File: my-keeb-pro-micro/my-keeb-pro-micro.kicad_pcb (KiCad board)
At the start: 2 copper layers, 190.5 x 95.2 mm, 108 parts, among them SW1 SW_Push, U1 ATmega32U4-AU, Y1 16MHz

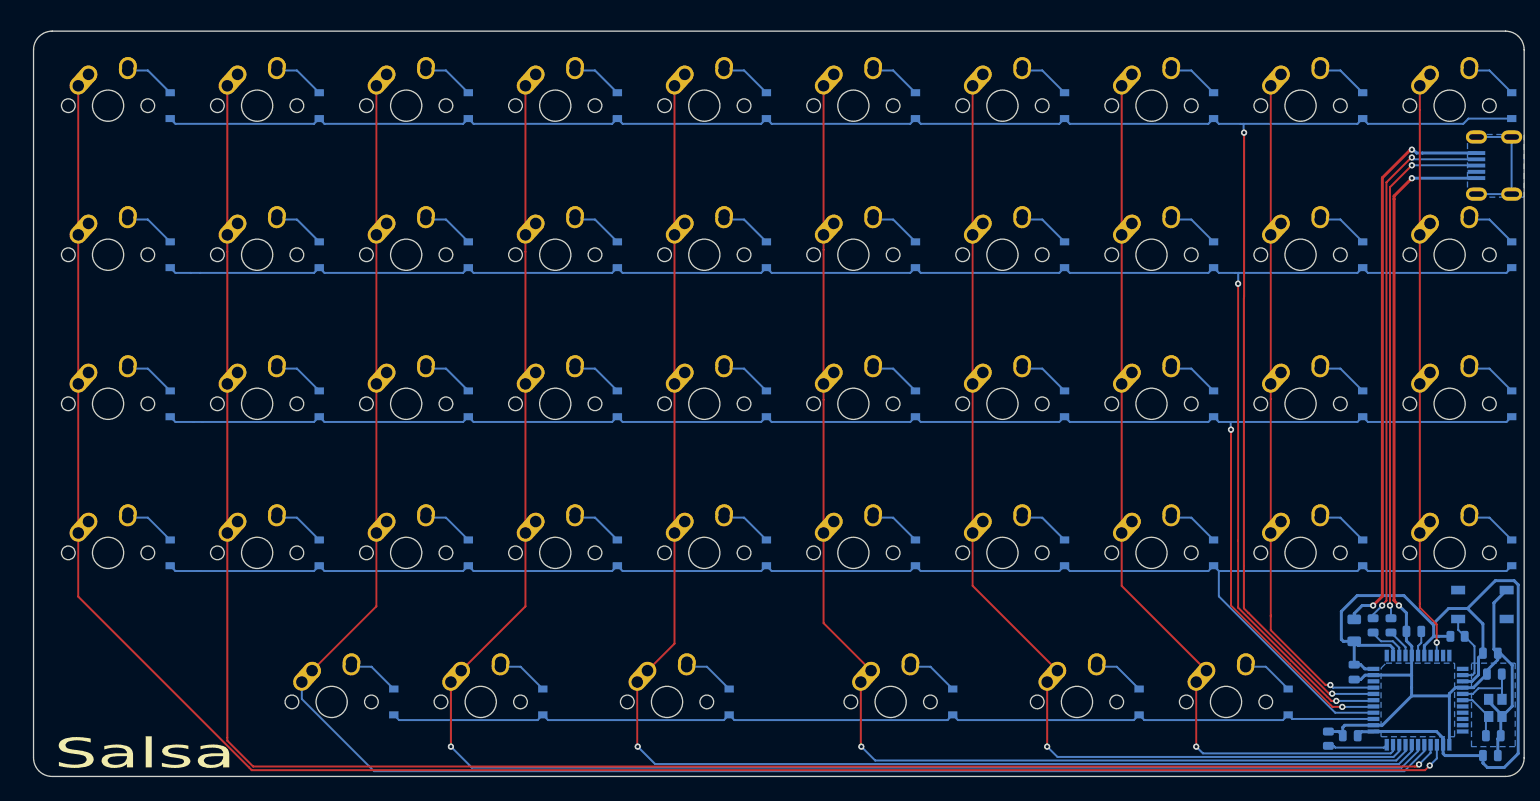
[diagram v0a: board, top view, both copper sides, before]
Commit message: Updated my-keeb pcb
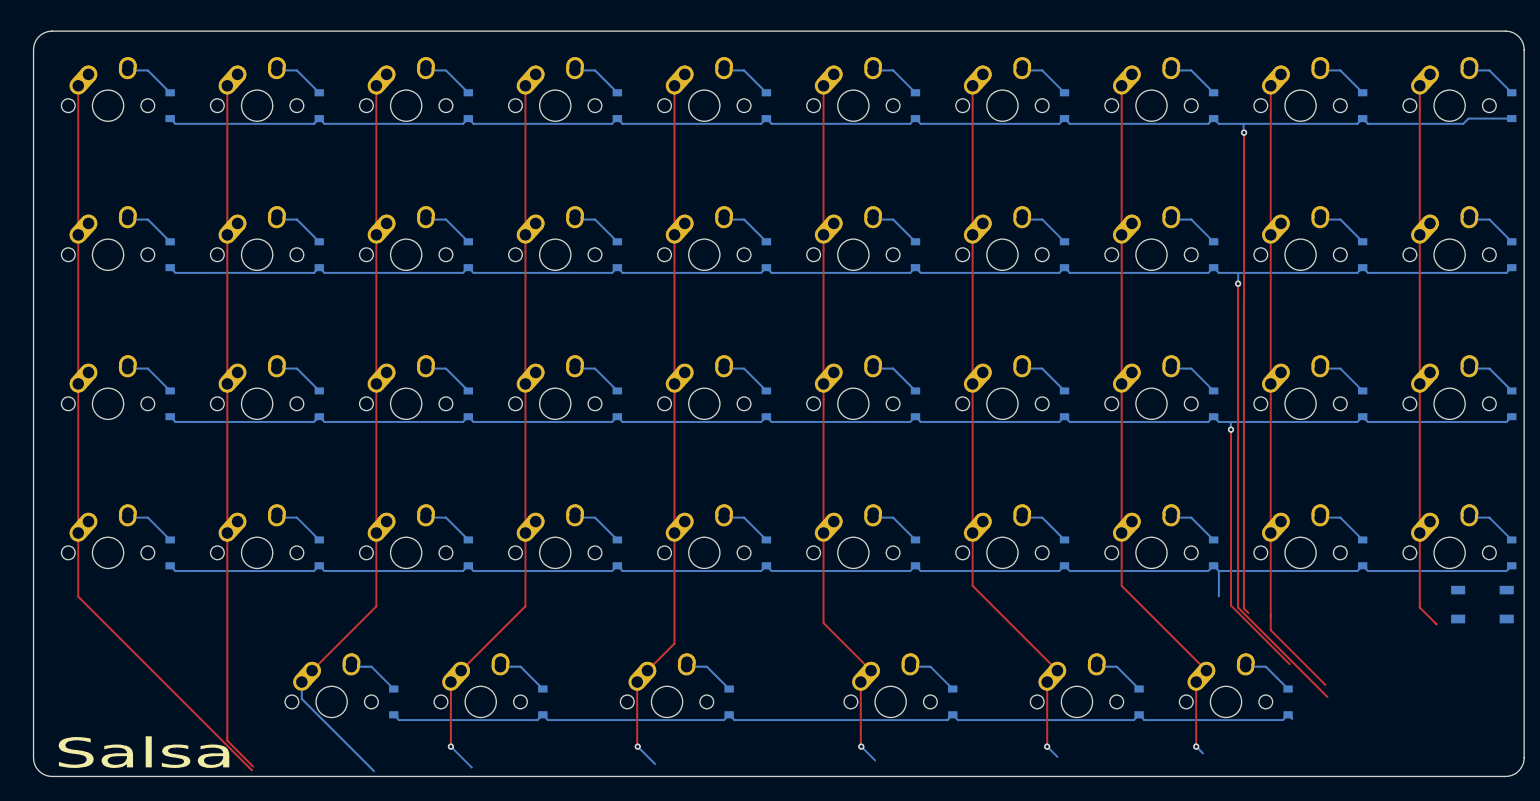
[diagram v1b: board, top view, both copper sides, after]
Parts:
- removed C1, C2, C5: 0.1uF, Capacitor_SMD:C_0805_2012Metric
- removed C3, C4: 22pF, Capacitor_SMD:C_0805_2012Metric
- removed C6: 1uF, Capacitor_SMD:C_0805_2012Metric
- removed C7: 10uF, Capacitor_SMD:C_0805_2012Metric
- removed F1: 500mA, Fuse:Fuse_1206_3216Metric
- removed R1, R2: 22, Resistor_SMD:R_0805_2012Metric
- removed R3, R4: 10k, Resistor_SMD:R_0805_2012Metric
- removed U1: ATmega32U4-AU, Package_QFP:TQFP-44_10x10mm_P0.8mm
- removed USB1: Molex-0548190589, random-keyboard-parts:Molex-0548190589
- removed Y1: 16MHz, Crystal:Crystal_SMD_3225-4Pin_3.2x2.5mm
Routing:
- net COL0: track 250.5 -> 96.6 mm, vias 1 -> 0
- net COL1: track 240.6 -> 88.4 mm, vias 1 -> 0
- net GND: track 144.9 -> 0.00 mm, vias 2 -> 0
- net COL2: track 229.5 -> 93.4 mm
- net COL3: track 212.8 -> 90.2 mm
- net +5V: track 110.1 -> 0.00 mm
- net COL4: track 185.8 -> 87.6 mm
- net VCC: track 72.6 -> 0.00 mm, vias 2 -> 0
- net D-: track 69.3 -> 0.00 mm, vias 2 -> 0
- net COL5: track 157.1 -> 88.0 mm
- net D+: track 67.4 -> 0.00 mm, vias 2 -> 0
- net COL6: track 134.2 -> 89.3 mm
- net ROW3: track 205.6 -> 179.7 mm
- net COL7: track 113.9 -> 88.7 mm
- net ROW0: track 259.5 -> 239.2 mm, vias 2 -> 1
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- removed copper zone on B.Cu, net GND

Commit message: Added pro micro to pcb, routing WIP
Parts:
- added U1: ProMicro, promicro:ProMicro, B.Cu at (117.5, 28.6)
- SW1: moved to F.Cu
- moved SW1 15.3 mm to (188.9, 98.4)
- moved D24 9.69 mm to (117.5, 27.8), turned to 0 degrees
- moved D25 9.69 mm to (117.5, 46.8), turned to 0 degrees
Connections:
- SW1 pad 1: GND -> Net-(SW1-Pad1)
- SW1 pad 2: Net-(R3-Pad2) -> GND
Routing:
- net ROW1: track 235.4 -> 239.2 mm
- net ROW0: track 239.2 -> 243.0 mm, vias 1 -> 3
- net Net-(D24-Pad2): track 6.62 -> 10.4 mm
- net Net-(D25-Pad2): track 6.62 -> 10.4 mm

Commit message: Added some footprints prettys
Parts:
- D45: footprint Diode_SMD:D_SOD-123 -> random-keyboard-parts:D_SOD-123-Pretty
- moved SW1 120.2 mm to (88.9, 31.8)
- moved D24 3.29 mm to (120.7, 26.9), turned to 90 degrees
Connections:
- U1 pad 19: ROW0 -> Net-(U1-Pad19)
- U1 pad 20: Net-(U1-Pad20) -> ROW0
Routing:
- net ROW0: track 243.0 -> 179.3 mm, vias 3 -> 0
- net ROW1: track 239.2 -> 180.3 mm, vias 1 -> 0
- net GND: track 0.00 -> 57.9 mm
- net Net-(SW1-Pad1): track 0.00 -> 40.3 mm
- net ROW2: track 210.5 -> 176.5 mm, vias 1 -> 0
- net COL8: track 79.5 -> 57.1 mm
- net Net-(D24-Pad2): track 10.4 -> 7.83 mm
- net Net-(U1-Pad19): track 0.00 -> 0.67 mm

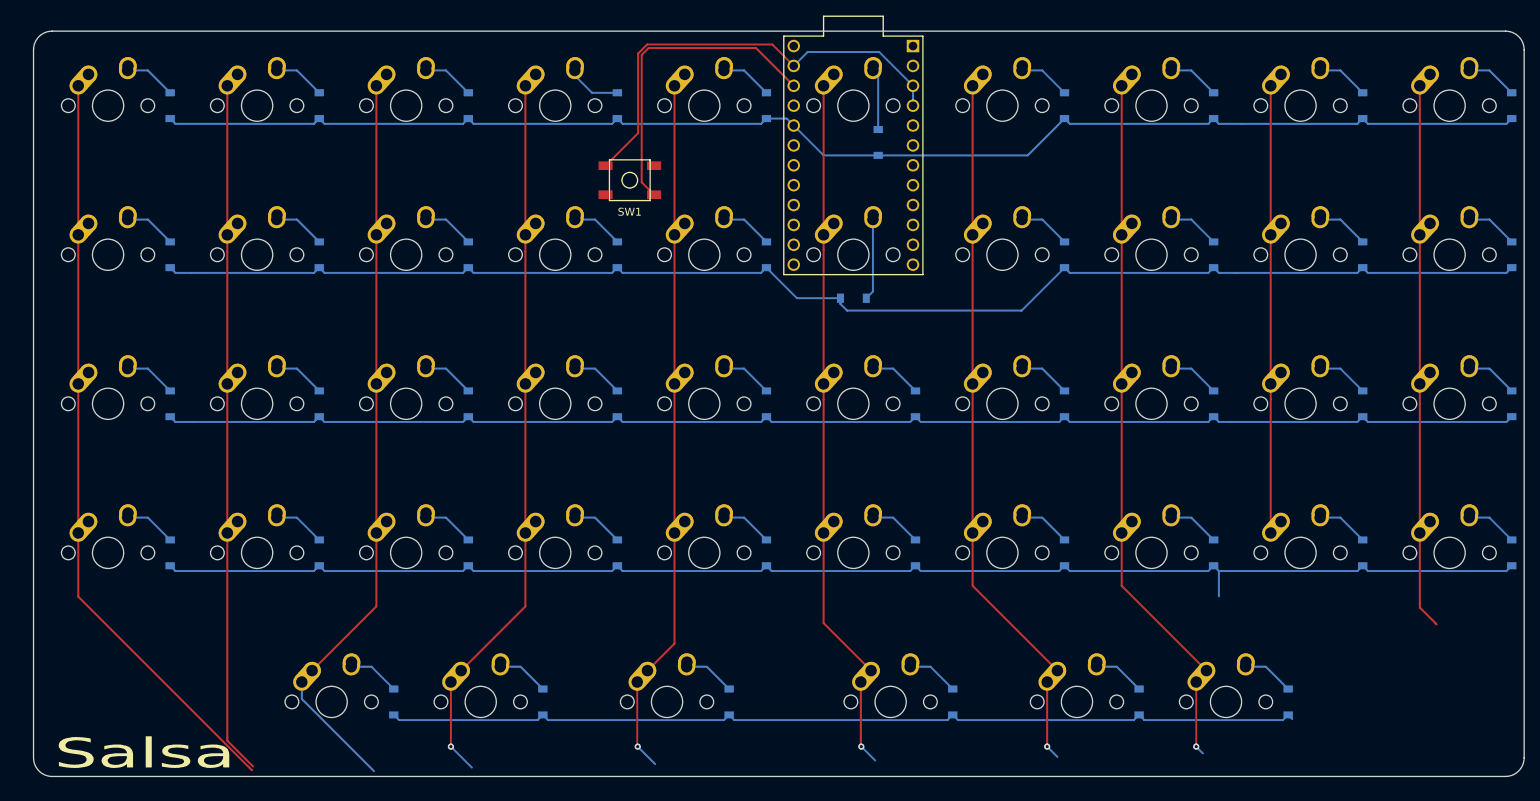
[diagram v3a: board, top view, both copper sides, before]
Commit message: Promicro pcb uses hybrid diodes
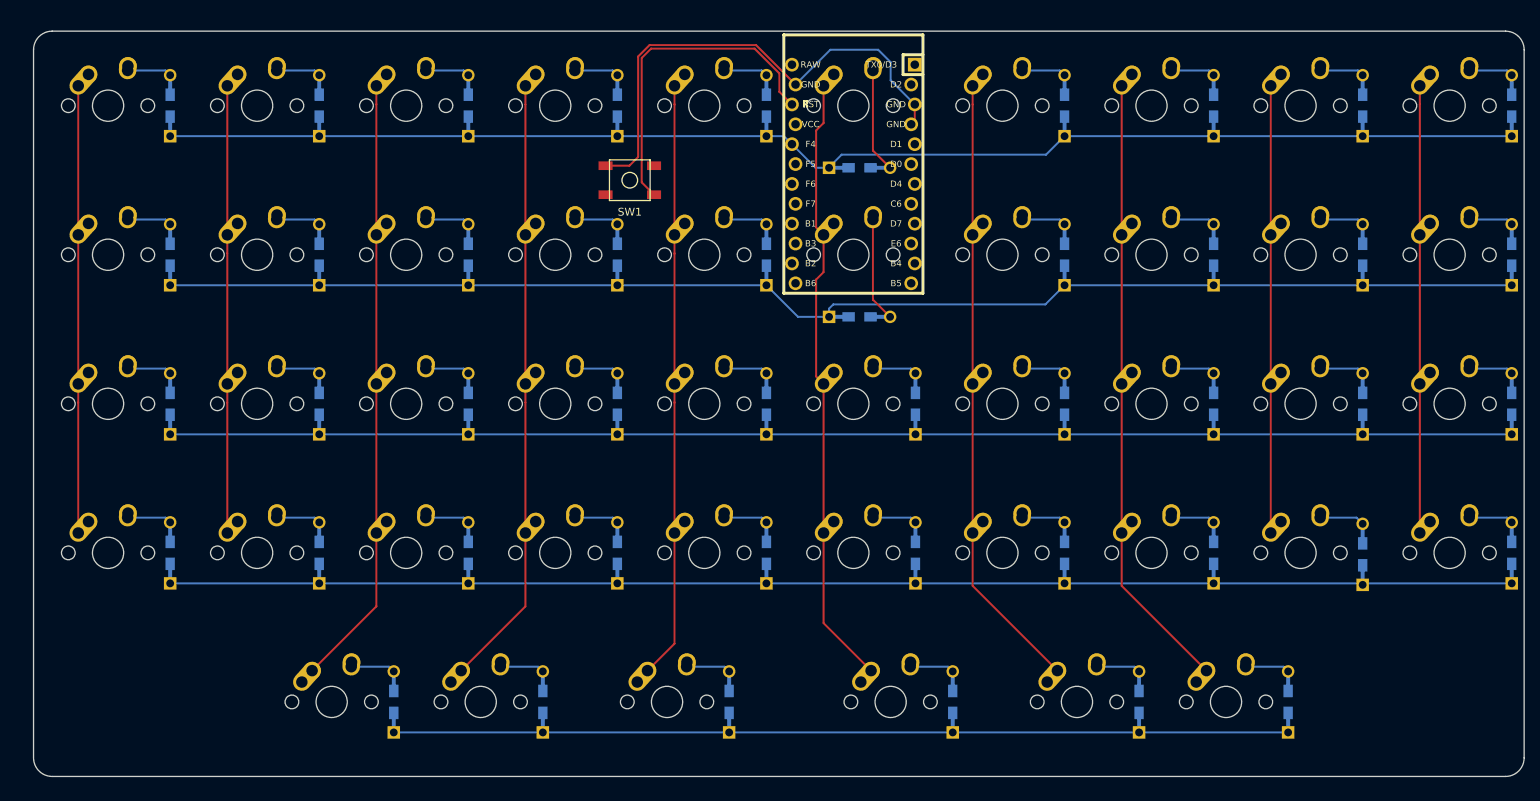
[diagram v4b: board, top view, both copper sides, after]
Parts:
- D1, D10, D11, D12, D13, D14, D15, D16, D17, D18, D19, D2, D20, D21, D22, D23, D24, D25, D26, D27, D28, D29, D3, D30, D31, D32, D33, D34, D35, D36, D37, D38, D39, D4, D40, D41, D42, D43, D44, D46, D5, D6, D7, D8, D9: footprint Diode_SMD:D_SOD-123 -> Keebio-Parts:Diode-Hybrid-Back; moved to F.Cu
- D45: footprint random-keyboard-parts:D_SOD-123-Pretty -> Keebio-Parts:Diode-Hybrid-Back; moved to F.Cu
- U1: footprint promicro:ProMicro -> Keebio-Parts:ArduinoProMicro-ZigZag
- moved D24 4.02 mm to (118.3, 30.2), turned to 180 degrees
- moved D25 2.51 mm to (118.3, 49.2), turned to 180 degrees
- moved U1 2.38 mm to (117.5, 31.0)
- moved D42 0.19 mm to (182.6, 79.6), turned to 270 degrees
- turned D1 to 270 degrees
- turned D10 to 270 degrees
- turned D11 to 270 degrees
- turned D12 to 270 degrees
- turned D13 to 270 degrees
- turned D14 to 270 degrees
- turned D15 to 270 degrees
- turned D16 to 270 degrees
- turned D17 to 270 degrees
- turned D18 to 270 degrees
- turned D19 to 270 degrees
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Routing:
- net COL0: track 96.6 -> 57.1 mm
- net COL1: track 88.4 -> 57.1 mm
- net COL2: track 93.4 -> 78.1 mm
- net COL9: track 69.7 -> 57.1 mm
- net COL3: track 90.2 -> 78.1 mm, vias 1 -> 0
- net COL4: track 87.6 -> 76.2 mm, vias 1 -> 0
- net COL6: track 89.3 -> 79.2 mm, vias 1 -> 0
- net COL7: track 88.7 -> 79.2 mm, vias 1 -> 0
- net COL5: track 88.0 -> 78.8 mm, vias 1 -> 0
- net ROW3: track 179.7 -> 171.5 mm
- net GND: track 57.9 -> 64.3 mm
- net Net-(D24-Pad2): track 7.83 -> 13.3 mm
- net ROW2: track 176.5 -> 171.5 mm
- net ROW1: track 180.3 -> 175.4 mm
- net ROW0: track 179.3 -> 174.8 mm
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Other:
- board text removed: "Salsa"

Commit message: Finished pro micro pcb
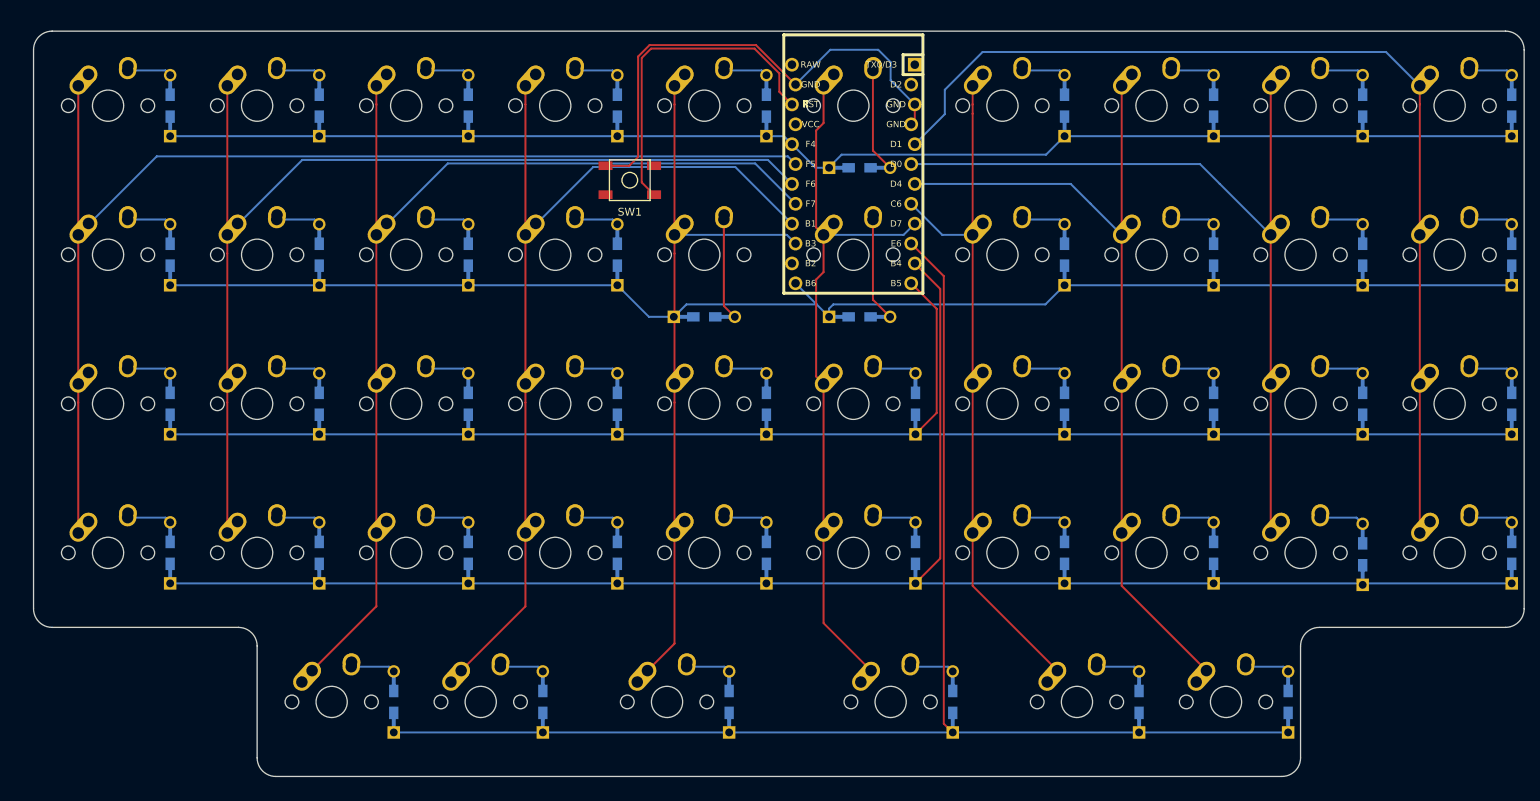
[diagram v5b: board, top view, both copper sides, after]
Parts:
- moved D20 11.2 mm to (98.4, 49.2), turned to 180 degrees
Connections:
- U1 pad 10: Net-(U1-Pad10) -> ROW4
- U1 pad 11: Net-(U1-Pad11) -> ROW3
- U1 pad 12: Net-(U1-Pad12) -> ROW2
- U1 pad 13: Net-(U1-Pad13) -> ROW1
- U1 pad 15: Net-(U1-Pad15) -> COL4
- U1 pad 16: Net-(U1-Pad16) -> COL3
- U1 pad 17: Net-(U1-Pad17) -> COL2
- U1 pad 18: Net-(U1-Pad18) -> COL1
- U1 pad 19: Net-(U1-Pad19) -> COL0
- U1 pad 5: Net-(U1-Pad5) -> COL9
- U1 pad 6: Net-(U1-Pad6) -> COL8
- U1 pad 7: Net-(U1-Pad7) -> COL7
- U1 pad 8: Net-(U1-Pad8) -> COL6
- U1 pad 9: Net-(U1-Pad9) -> COL5
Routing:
- net COL0: track 57.1 -> 153.4 mm
- net COL1: track 57.1 -> 134.6 mm
- net COL9: track 57.1 -> 130.2 mm
- net ROW4: track 114.3 -> 179.1 mm
- net COL2: track 78.1 -> 137.6 mm
- net COL8: track 57.1 -> 106.8 mm
- net ROW3: track 171.5 -> 215.0 mm
- net COL3: track 78.1 -> 118.8 mm
- net COL7: track 79.2 -> 108.4 mm
- net ROW2: track 171.5 -> 193.2 mm
- net COL4: track 76.2 -> 92.1 mm
- net COL5: track 78.8 -> 91.1 mm
- net COL6: track 79.2 -> 88.8 mm
- net Net-(D20-Pad2): track 5.69 -> 13.0 mm
- net ROW1: track 175.4 -> 180.6 mm
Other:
- outline, holes or cut-outs redrawn

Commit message: Fixed track issues
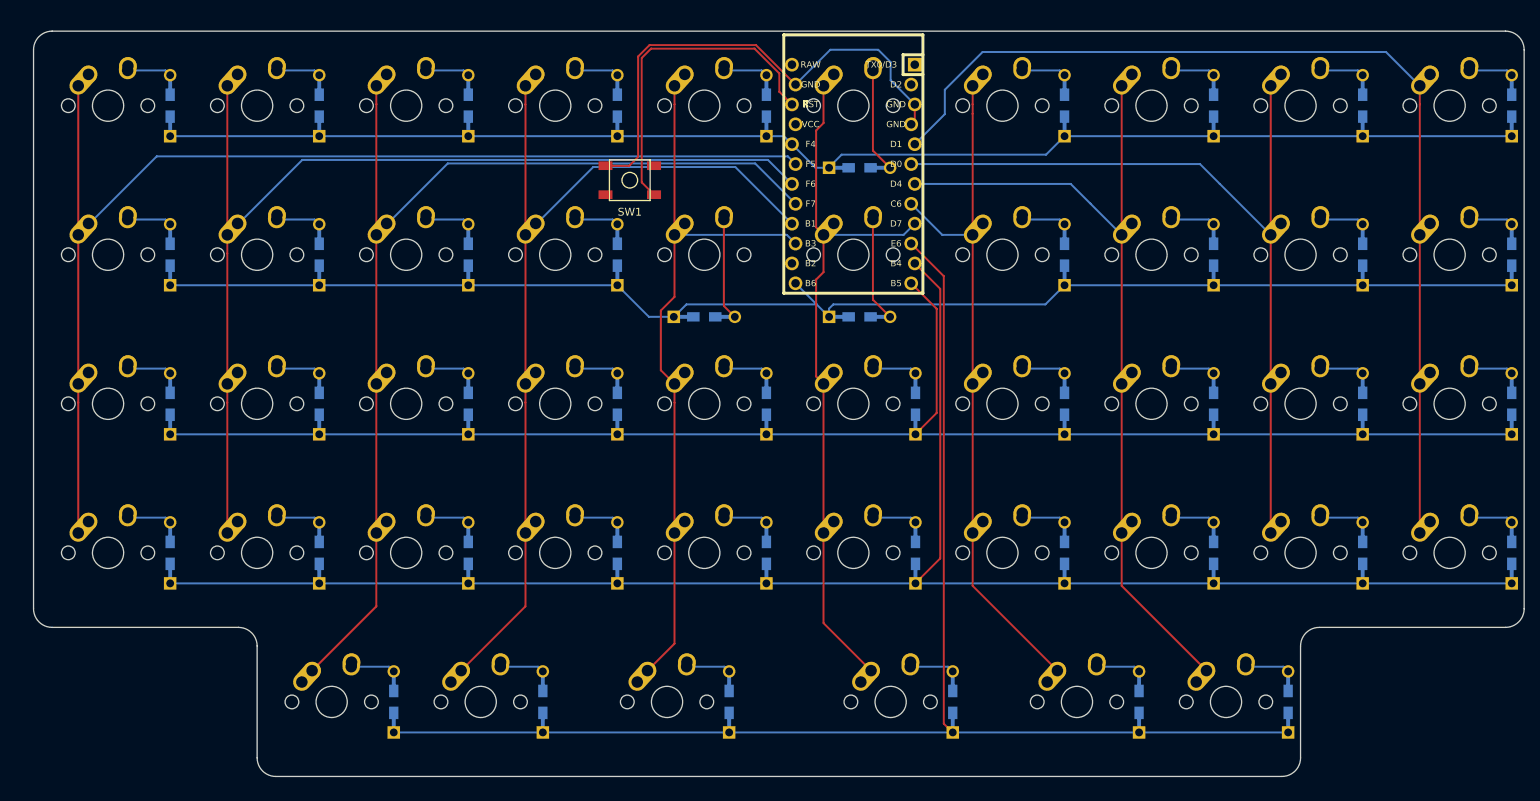
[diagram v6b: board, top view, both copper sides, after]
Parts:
- moved D42 0.19 mm to (182.6, 79.4)
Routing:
- net COL4: track 92.1 -> 93.5 mm
